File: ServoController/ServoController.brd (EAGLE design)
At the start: 31.8 x 50.8 mm, 9 parts

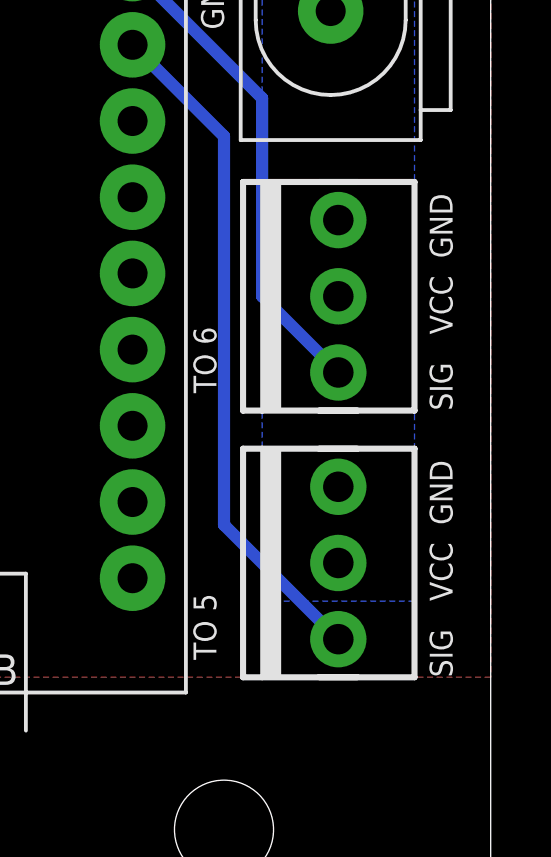
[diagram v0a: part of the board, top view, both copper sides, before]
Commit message: Add more documentation via silkscreen
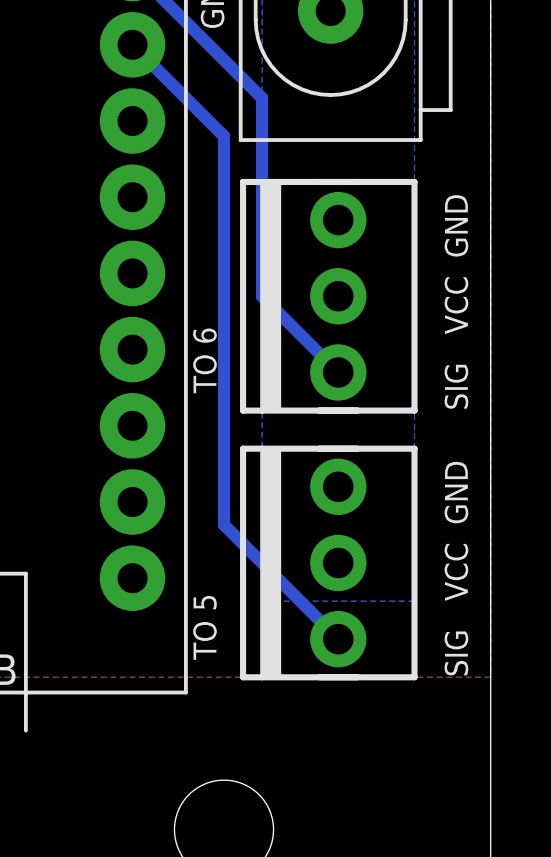
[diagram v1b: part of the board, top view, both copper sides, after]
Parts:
- moved U$2 9.24 mm to (15.5, 44.2), turned to 90 degrees
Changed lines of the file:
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@@
 <wire x1="31.75" y1="50.8" x2="0" y2="50.8" width="0" layer="20"/>
 <wire x1="0" y1="50.8" x2="0" y2="0" width="0" layer="20"/>
-<text x="30.48" y="22.86" size="0.762" layer="25" font="vector" rot="R90">GND</text>
-<text x="30.48" y="13.97" size="0.762" layer="25" font="vector" rot="R90">GND</text>
+<text x="30.988" y="22.86" size="0.762" layer="25" font="vector" rot="R90">GND</text>
+<text x="30.988" y="13.97" size="0.762" layer="25" font="vector" rot="R90">GND</text>
 <text x="22.86" y="30.48" size="0.762" layer="21" font="vector" rot="R90">GND</text>
 <text x="22.098" y="39.624" size="0.762" layer="21" font="vector" rot="R270">VCC</text>
-<text x="30.48" y="20.32" size="0.762" layer="25" font="vector" rot="R90">VCC</text>
-<text x="30.48" y="11.43" size="0.762" layer="25" font="vector" rot="R90">VCC</text>
-<text x="30.48" y="17.78" size="0.762" layer="25" font="vector" rot="R90">SIG</text>
-<text x="30.48" y="8.89" size="0.762" layer="25" font="vector" rot="R90">SIG</text>
-<text x="12.954" y="10.16" size="0.762" layer="26" font="vector" rot="MR90">(c) Pioneers In Engineering
+<text x="30.988" y="20.32" size="0.762" layer="25" font="vector" rot="R90">VCC</text>
+<text x="30.988" y="11.43" size="0.762" layer="25" font="vector" rot="R90">VCC</text>
+<text x="30.988" y="17.78" size="0.762" layer="25" font="vector" rot="R90">SIG</text>
+<text x="30.988" y="8.89" size="0.762" layer="25" font="vector" rot="R90">SIG</text>
+<text x="6.858" y="1.27" size="1.27" layer="26" font="vector" rot="MR90">(c) Pioneers In Engineering
 Design by: Seiya Ono, Catherine Kim
 This design is open source hardware.
@@
 <attribute name="VALUE" x="31.115" y="17.78" size="1.27" layer="27" font="vector" rot="R90"/>
 </element>
-<element name="U$2" library="pie" package="PIE-LOGO-SMALL" value="" x="10.668" y="36.322" rot="MR270"/>
+<element name="U$2" library="pie" package="PIE-LOGO-SMALL" value="" x="15.494" y="44.196" rot="MR90"/>
 <element name="U$1" library="pie" package="STAND-OFF" value="" x="22.86" y="46.482"/>
 <element name="U$3" library="pie" package="STAND-OFF" value="" x="3.81" y="3.81"/>

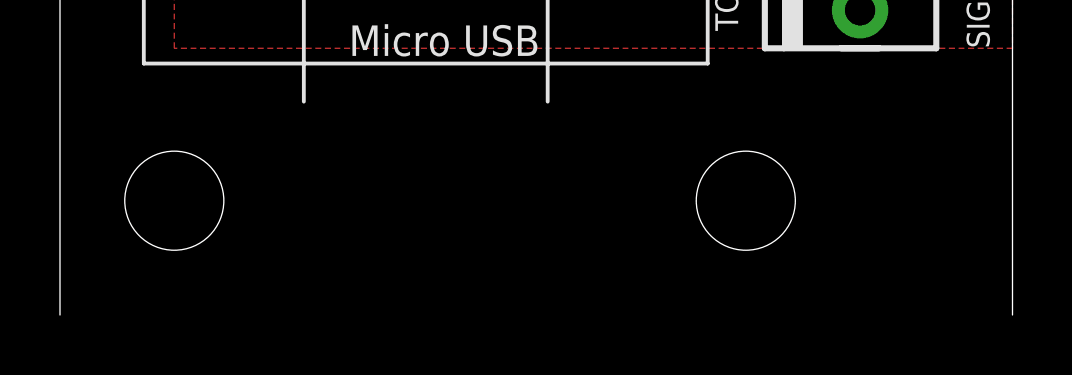
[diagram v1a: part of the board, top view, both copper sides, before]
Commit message: Move around silkscreen
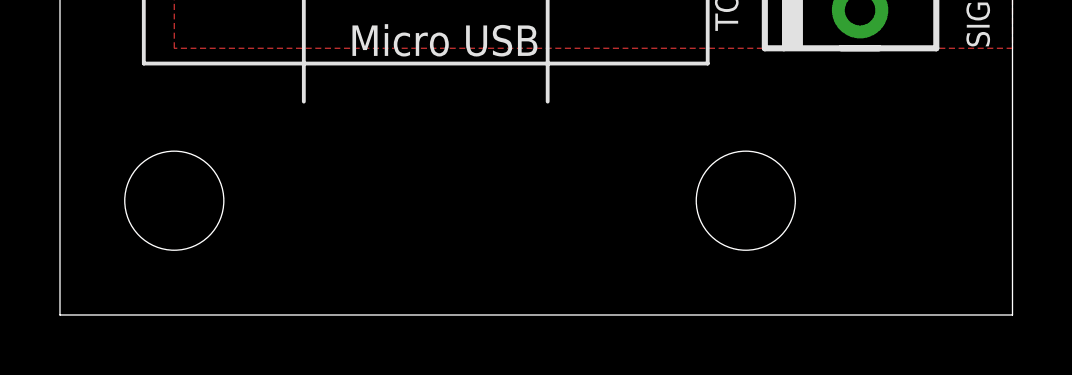
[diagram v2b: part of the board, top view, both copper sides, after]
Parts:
- added U$6: (no value), pie:OSHW-LOGO-S
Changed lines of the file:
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@@
 <board>
 <plain>
-<wire x1="0" y1="0" x2="31.75" y2="0" width="0" layer="26"/>
+<wire x1="0" y1="0" x2="31.75" y2="0" width="0" layer="20"/>
 <wire x1="31.75" y1="0" x2="31.75" y2="50.8" width="0" layer="20"/>
 <wire x1="31.75" y1="50.8" x2="0" y2="50.8" width="0" layer="20"/>
@@
 <element name="JP3" library="pie" package="ATX" value="ATX" x="26.416" y="34.798" rot="R270"/>
 <element name="U$5" library="pie" package="STAND-OFF" value="" x="22.86" y="3.81"/>
+<element name="U$6" library="pie" package="OSHW-LOGO-S" value="" x="8.128" y="39.878" rot="MR90"/>
 </elements>
 <signals>
